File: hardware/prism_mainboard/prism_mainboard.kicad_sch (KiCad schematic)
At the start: 0 parts

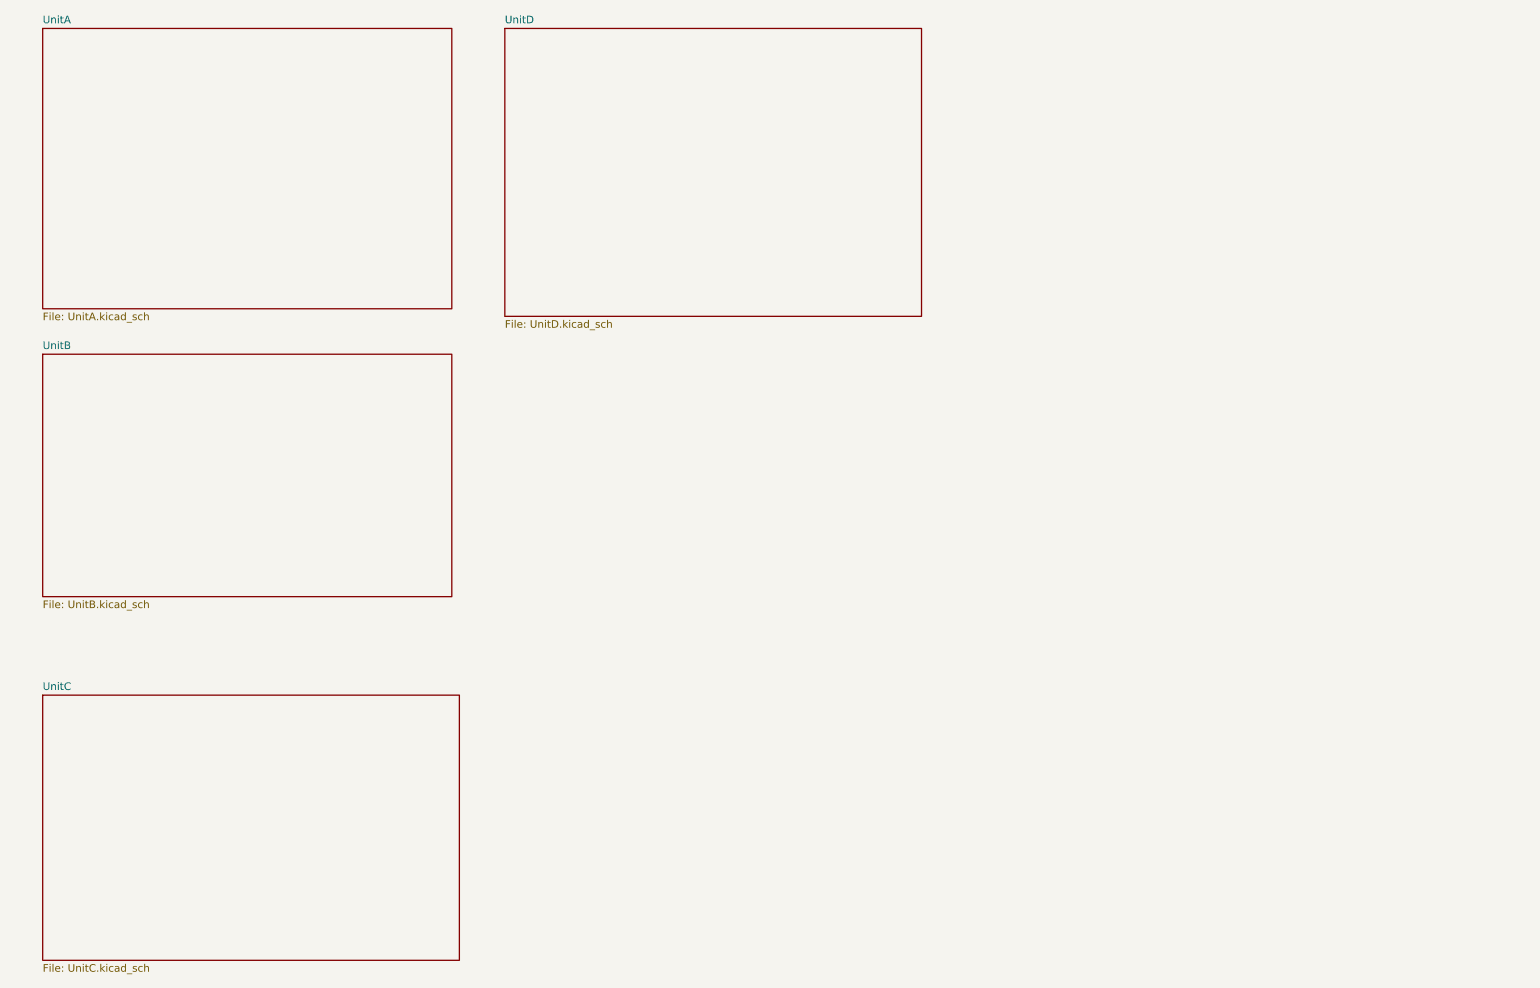
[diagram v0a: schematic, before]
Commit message: KiCAD and Datasheet Updates
Updated KiCAD added LMS7002M Transceiver, added power systems sheet, added LMS7002M Datasheets and PCB sheet for XC7Z010
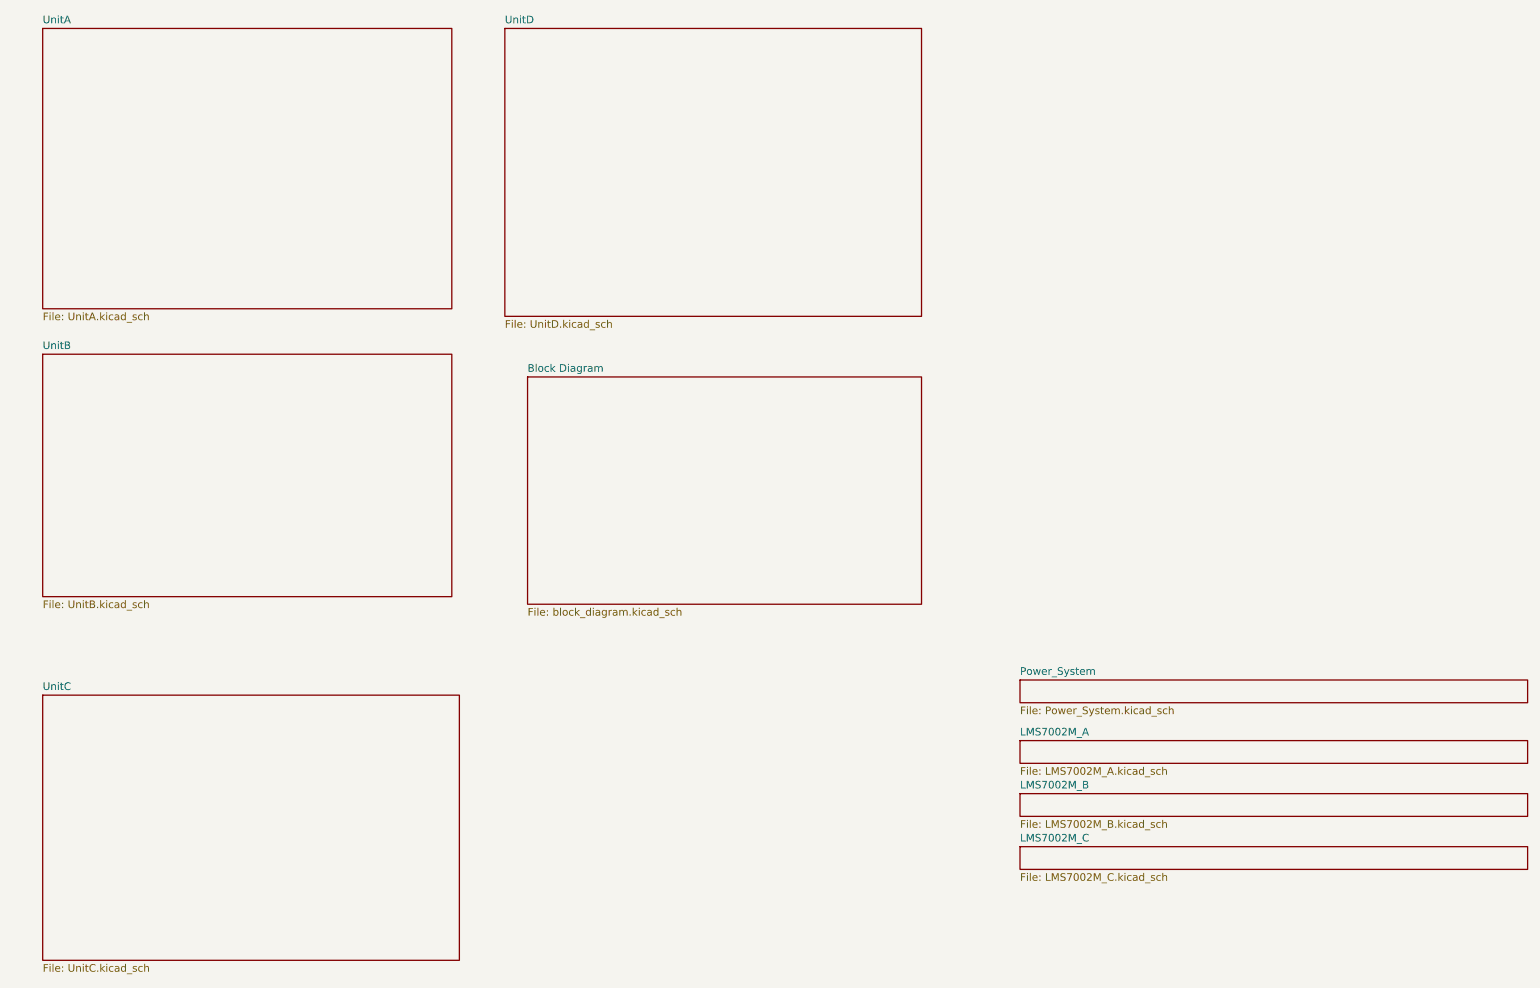
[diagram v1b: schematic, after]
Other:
- added sheet Block Diagram (block_diagram.kicad_sch)
- added sheet LMS7002M_A (LMS7002M_A.kicad_sch)
- added sheet LMS7002M_B (LMS7002M_B.kicad_sch)
- added sheet LMS7002M_C (LMS7002M_C.kicad_sch)
- added sheet Power_System (Power_System.kicad_sch)
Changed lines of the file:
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@@
+	)
+	(sheet
+		(at 187.96 130.81)
+		(size 85.09 3.81)
+		(exclude_from_sim no)
+		(in_bom yes)
+		(on_board yes)
+		(dnp no)
+		(fields_autoplaced yes)
+		(stroke
+			(width 0.1524)
+			(type solid)
+		)
+		(fill
+			(color 0 0 0 0.0000)
+		)
+		(property "Sheetname" "Power_System"
+			(at 187.96 130.0984 0)
+			(effects
+				(font
+					(size 1.27 1.27)
+				)
+				(justify left bottom)
+			)
+		)
+		(property "Sheetfile" "Power_System.kicad_sch"
+			(at 187.96 135.2046 0)
+			(effects
+				(font
+					(size 1.27 1.27)
+				)
+				(justify left top)
+			)
+		)
+		(instances
+			(project "prism_mainboard"
+				(path "/1d5f25f9-3e6f-41df-a8ec-41fc885bea9a"
+					(page "7")
+				)
+			)
+		)
 	)
 	(sheet
@@
 			(project "prism_mainboard"
 				(path "/1d5f25f9-3e6f-41df-a8ec-41fc885bea9a"
-					(page "3")
+					(page "4")
 				)
 			)
@@
 			(project "prism_mainboard"
 				(path "/1d5f25f9-3e6f-41df-a8ec-41fc885bea9a"
-					(page "4")
+					(page "5")
 				)
 			)
@@
 			(project "prism_mainboard"
 				(path "/1d5f25f9-3e6f-41df-a8ec-41fc885bea9a"
+					(page "3")
+				)
+			)
+		)
+	)
+	(sheet
+		(at 187.96 158.75)
+		(size 85.09 3.81)
+		(exclude_from_sim no)
+		(in_bom yes)
+		(on_board yes)
+		(dnp no)
+		(fields_autoplaced yes)
+		(stroke
+			(width 0.1524)
+			(type solid)
+		)
+		(fill
+			(color 0 0 0 0.0000)
+		)
+		(property "Sheetname" "LMS7002M_C"
+			(at 187.96 158.0384 0)
+			(effects
+				(font
+					(size 1.27 1.27)
+				)
+				(justify left bottom)
+			)
+		)
+		(property "Sheetfile" "LMS7002M_C.kicad_sch"
+			(at 187.96 163.1446 0)
+			(effects
+				(font
+					(size 1.27 1.27)
+				)
+				(justify left top)
+			)
+		)
+		(instances
+			(project "prism_mainboard"
+				(path "/1d5f25f9-3e6f-41df-a8ec-41fc885bea9a"
+					(page "10")
+				)
+			)
+		)
+	)
+	(sheet
+		(at 187.96 140.97)
+		(size 85.09 3.81)
+		(exclude_from_sim no)
+		(in_bom yes)
+		(on_board yes)
+		(dnp no)
+		(fields_autoplaced yes)
+		(stroke
+			(width 0.1524)
+			(type solid)
+		)
+		(fill
+			(color 0 0 0 0.0000)
+		)
+		(property "Sheetname" "LMS7002M_A"
+			(at 187.96 140.2584 0)
+			(effects
+				(font
+					(size 1.27 1.27)
+				)
+				(justify left bottom)
+			)
+		)
+		(property "Sheetfile" "LMS7002M_A.kicad_sch"
+			(at 187.96 145.3646 0)
+			(effects
+				(font
+					(size 1.27 1.27)
+				)
+				(justify left top)
+			)
+		)
+		(instances
+			(project "prism_mainboard"
+				(path "/1d5f25f9-3e6f-41df-a8ec-41fc885bea9a"
+					(page "8")
+				)
+			)
+		)
+	)
+	(sheet
+		(at 105.41 80.01)
+		(size 66.04 38.1)
+		(exclude_from_sim no)
+		(in_bom yes)
+		(on_board yes)
+		(dnp no)
+		(fields_autoplaced yes)
+		(stroke
+			(width 0.1524)
+			(type solid)
+		)
+		(fill
+			(color 0 0 0 0.0000)
+		)
+		(property "Sheetname" "Block Diagram"
+			(at 105.41 79.2984 0)
+			(effects
+				(font
+					(size 1.27 1.27)
+				)
+				(justify left bottom)
+			)
+		)
+		(property "Sheetfile" "block_diagram.kicad_sch"
+			(at 105.41 118.6946 0)
+			(effects
+				(font
+					(size 1.27 1.27)
+				)
+				(justify left top)
+			)
+		)
+		(instances
+			(project "prism_mainboard"
+				(path "/1d5f25f9-3e6f-41df-a8ec-41fc885bea9a"
 					(page "2")
 				)
@@
 			(project "prism_mainboard"
 				(path "/1d5f25f9-3e6f-41df-a8ec-41fc885bea9a"
-					(page "5")
-				)
-			)
+					(page "6")
+				)
+			)
+		)
+	)
+	(sheet
+		(at 187.96 149.86)
+		(size 85.09 3.81)
+		(exclude_from_sim no)
+		(in_bom yes)
+		(on_board yes)
+		(dnp no)
+		(fields_autoplaced yes)
+		(stroke
+			(width 0.1524)
+			(type solid)
+		)
+		(fill
+			(color 0 0 0 0.0000)
+		)
+		(property "Sheetname" "LMS7002M_B"
+			(at 187.96 149.1484 0)
+			(effects
+				(font
+					(size 1.27 1.27)
+				)
+				(justify left bottom)
+			)
+		)
+		(property "Sheetfile" "LMS7002M_B.kicad_sch"
+			(at 187.96 154.2546 0)
+			(effects
+				(font
+					(size 1.27 1.27)
+				)
+				(justify left top)
+			)
+		)
+		(instances
+			(project "prism_mainboard"
+				(path "/1d5f25f9-3e6f-41df-a8ec-41fc885bea9a"
+					(page "9")
+				)
+			)

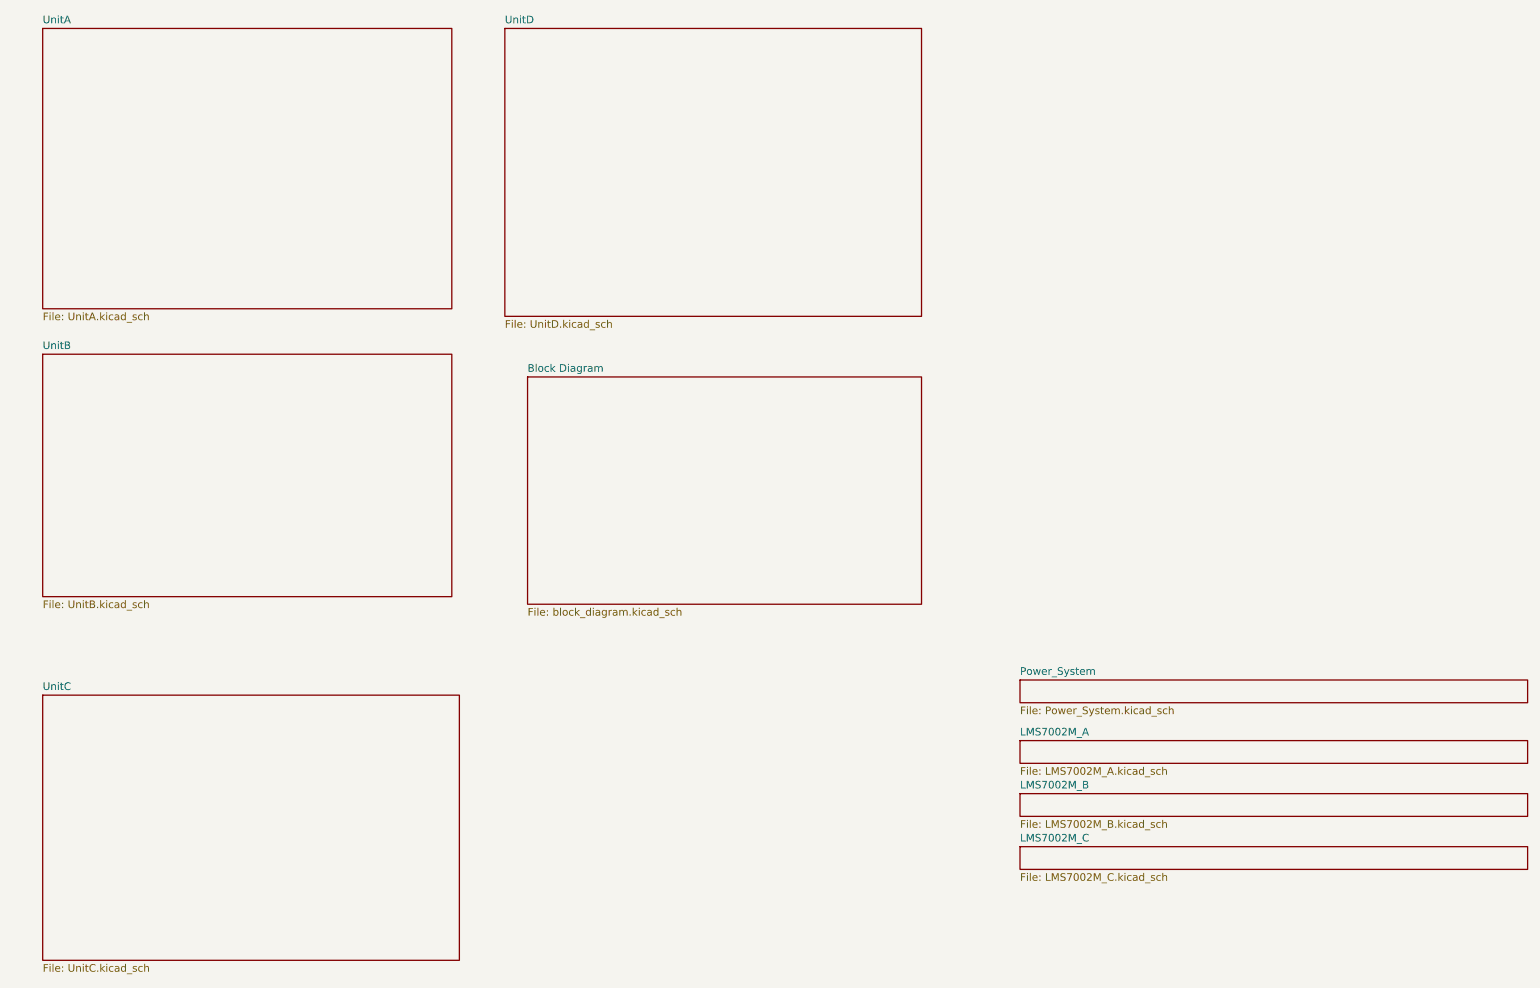
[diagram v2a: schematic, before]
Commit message: Schematics
More schematics updates, moving to Desktop for editing. Continued with power usage, debating use of Dedicated DDR3/3L power IC instead of using LDO and Buck from mainboard power.
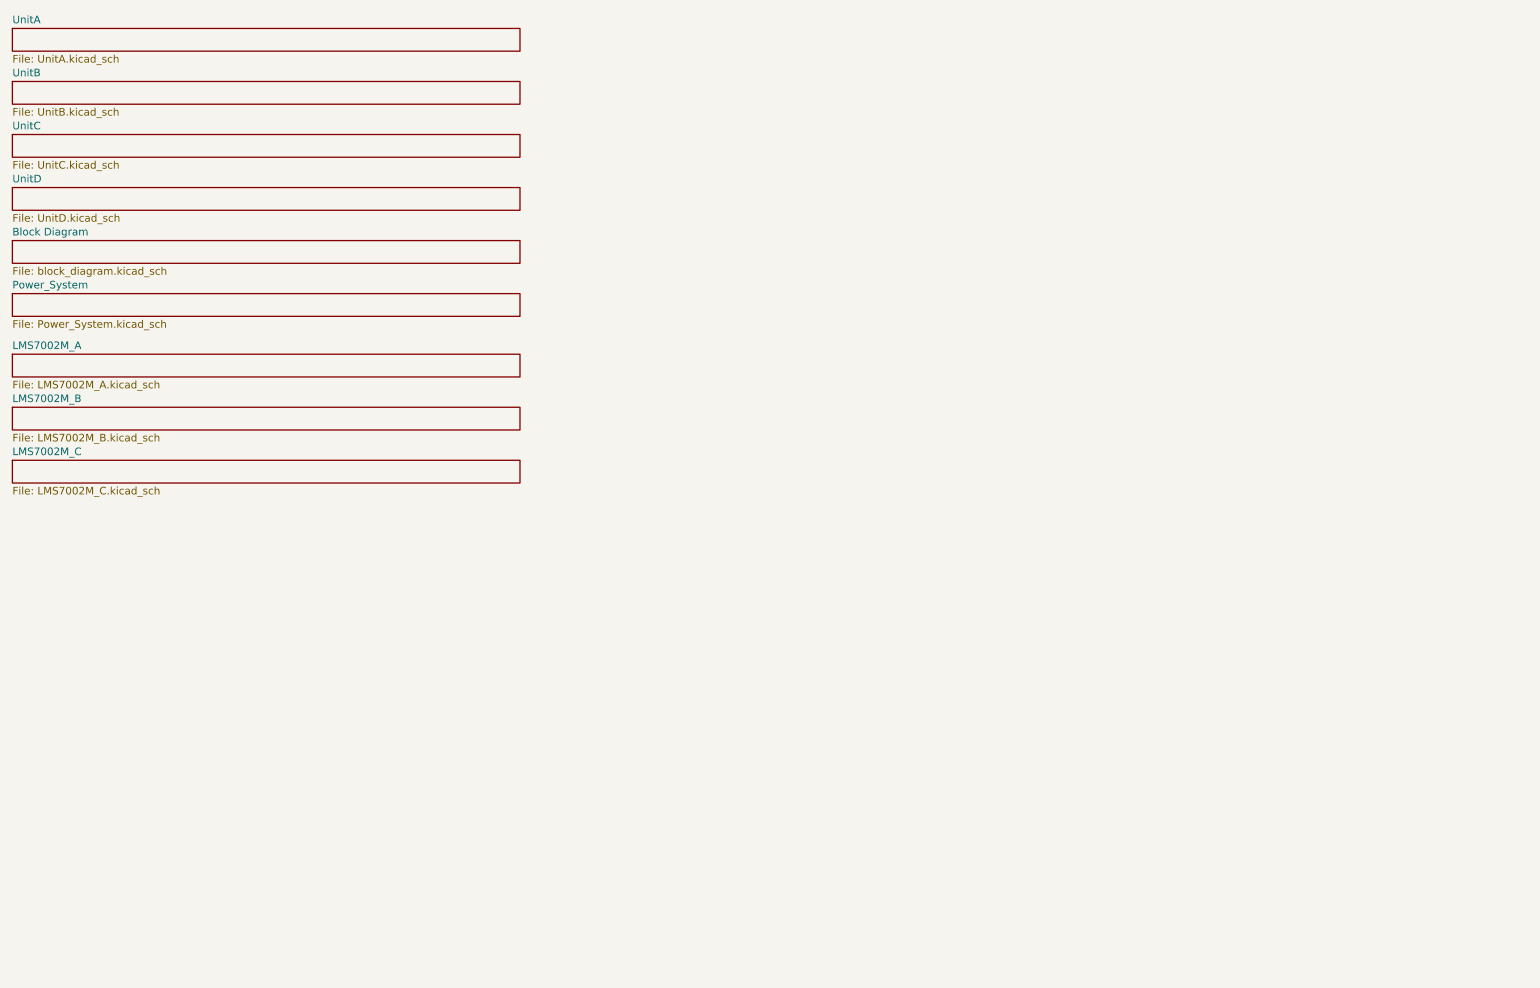
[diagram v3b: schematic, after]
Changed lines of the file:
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@@
 	)
 	(sheet
-		(at 187.96 130.81)
+		(at 19.05 66.04)
 		(size 85.09 3.81)
 		(exclude_from_sim no)
@@
 		)
 		(property "Sheetname" "Power_System"
-			(at 187.96 130.0984 0)
+			(at 19.05 65.3284 0)
 			(show_name no)
 			(do_not_autoplace no)
@@
 		)
 		(property "Sheetfile" "Power_System.kicad_sch"
-			(at 187.96 135.2046 0)
+			(at 19.05 70.4346 0)
 			(show_name no)
 			(do_not_autoplace no)
@@
 	)
 	(sheet
-		(at 24.13 76.2)
-		(size 68.58 40.64)
+		(at 19.05 30.48)
+		(size 85.09 3.81)
 		(exclude_from_sim no)
 		(in_bom yes)
@@
 		)
 		(property "Sheetname" "UnitB"
-			(at 24.13 75.4884 0)
+			(at 19.05 29.7684 0)
 			(show_name no)
 			(do_not_autoplace no)
@@
 		)
 		(property "Sheetfile" "UnitB.kicad_sch"
-			(at 24.13 117.4246 0)
+			(at 19.05 34.8746 0)
 			(show_name no)
 			(do_not_autoplace no)
@@
 		)
 		(property "Field2" ""
-			(at 24.13 76.2 0)
+			(at 19.05 30.48 0)
 			(show_name no)
 			(do_not_autoplace no)
@@
 	)
 	(sheet
-		(at 24.13 133.35)
-		(size 69.85 44.45)
+		(at 19.05 39.37)
+		(size 85.09 3.81)
 		(exclude_from_sim no)
 		(in_bom yes)
@@
 		)
 		(property "Sheetname" "UnitC"
-			(at 24.13 132.6384 0)
+			(at 19.05 38.6584 0)
 			(show_name no)
 			(do_not_autoplace no)
@@
 		)
 		(property "Sheetfile" "UnitC.kicad_sch"
-			(at 24.13 178.3846 0)
+			(at 19.05 43.7646 0)
 			(show_name no)
 			(do_not_autoplace no)
@@
 	)
 	(sheet
-		(at 24.13 21.59)
-		(size 68.58 46.99)
+		(at 19.05 21.59)
+		(size 85.09 3.81)
 		(exclude_from_sim no)
 		(in_bom yes)
@@
 		)
 		(property "Sheetname" "UnitA"
-			(at 24.13 20.8784 0)
+			(at 19.05 20.8784 0)
 			(show_name yes)
 			(do_not_autoplace no)
@@
 		)
 		(property "Sheetfile" "UnitA.kicad_sch"
-			(at 24.13 69.1646 0)
+			(at 19.05 25.9846 0)
 			(show_name no)
 			(do_not_autoplace no)
@@
 	)
 	(sheet
-		(at 187.96 158.75)
+		(at 19.05 93.98)
 		(size 85.09 3.81)
 		(exclude_from_sim no)
@@
 		)
 		(property "Sheetname" "LMS7002M_C"
-			(at 187.96 158.0384 0)
+			(at 19.05 93.2684 0)
 			(show_name no)
 			(do_not_autoplace no)
@@
 		)
 		(property "Sheetfile" "LMS7002M_C.kicad_sch"
-			(at 187.96 163.1446 0)
+			(at 19.05 98.3746 0)
 			(show_name no)
 			(do_not_autoplace no)
@@
 	)
 	(sheet
-		(at 187.96 140.97)
+		(at 19.05 76.2)
 		(size 85.09 3.81)
 		(exclude_from_sim no)
@@
 		)
 		(property "Sheetname" "LMS7002M_A"
-			(at 187.96 140.2584 0)
+			(at 19.05 75.4884 0)
 			(show_name no)
 			(do_not_autoplace no)
@@
 		)
 		(property "Sheetfile" "LMS7002M_A.kicad_sch"
-			(at 187.96 145.3646 0)
+			(at 19.05 80.5946 0)
 			(show_name no)
 			(do_not_autoplace no)
@@
 	)
 	(sheet
-		(at 105.41 80.01)
-		(size 66.04 38.1)
+		(at 19.05 57.15)
+		(size 85.09 3.81)
 		(exclude_from_sim no)
 		(in_bom yes)
@@
 		)
 		(property "Sheetname" "Block Diagram"
-			(at 105.41 79.2984 0)
+			(at 19.05 56.4384 0)
 			(show_name no)
 			(do_not_autoplace no)
@@
 		)
 		(property "Sheetfile" "block_diagram.kicad_sch"
-			(at 105.41 118.6946 0)
+			(at 19.05 61.5446 0)
 			(show_name no)
 			(do_not_autoplace no)
@@
 	)
 	(sheet
-		(at 101.6 21.59)
-		(size 69.85 48.26)
+		(at 19.05 48.26)
+		(size 85.09 3.81)
 		(exclude_from_sim no)
 		(in_bom yes)
@@
 		)
 		(property "Sheetname" "UnitD"
-			(at 101.6 20.8784 0)
+			(at 19.05 47.5484 0)
 			(show_name no)
 			(do_not_autoplace no)
@@
 		)
 		(property "Sheetfile" "UnitD.kicad_sch"
-			(at 101.6 70.4346 0)
+			(at 19.05 52.6546 0)
 			(show_name no)
 			(do_not_autoplace no)
@@
 	)
 	(sheet
-		(at 187.96 149.86)
+		(at 19.05 85.09)
 		(size 85.09 3.81)
 		(exclude_from_sim no)
@@
 		)
 		(property "Sheetname" "LMS7002M_B"
-			(at 187.96 149.1484 0)
+			(at 19.05 84.3784 0)
 			(show_name no)
 			(do_not_autoplace no)
@@
 		)
 		(property "Sheetfile" "LMS7002M_B.kicad_sch"
-			(at 187.96 154.2546 0)
-			(show_name no)
-			(do_not_autoplace no)
+			(at 19.05 89.4846 0)
+			(show_name no)
+			(do_not_autoplace no)
